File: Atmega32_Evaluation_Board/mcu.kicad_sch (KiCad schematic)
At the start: 15 parts, among them SW1 RESET, U3 ATmega32A-A, Y1 16MHz

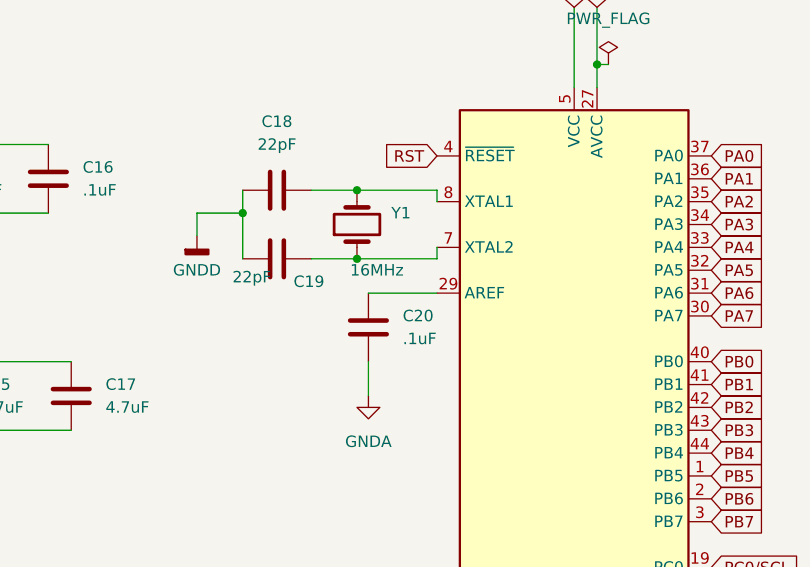
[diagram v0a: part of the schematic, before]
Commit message: added Atmega project
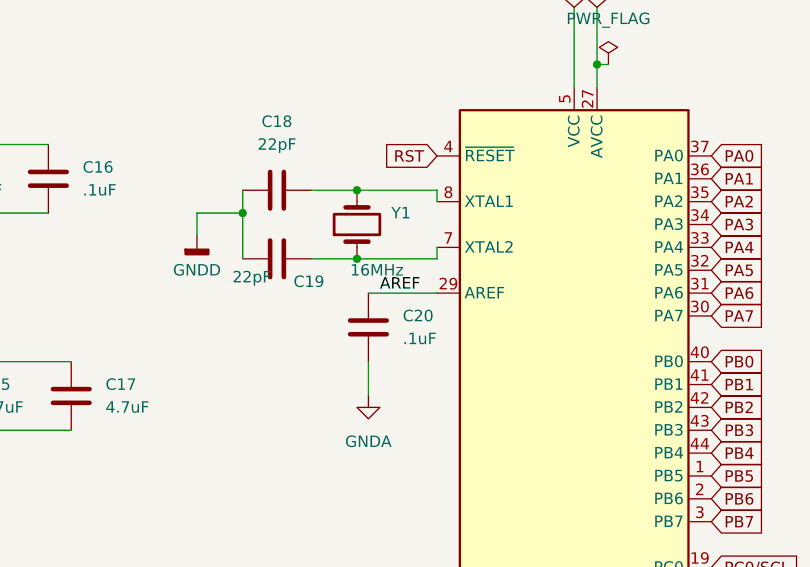
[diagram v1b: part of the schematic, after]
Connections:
- net AREF: now reaches C20.1, U3.29 (AREF)
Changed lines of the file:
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@@
+		)
+	)
+	(label "AREF"
+		(at 172.72 59.69 0)
+		(effects
+			(font
+				(size 1.27 1.27)
+			)
+			(justify left bottom)
 		)
 	)
